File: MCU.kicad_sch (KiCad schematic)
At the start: 19 parts, among them IC3 MT2492, J1 FH34SRJ-8S-0.5SH_50_, U17 LD1117S33TR_SOT223

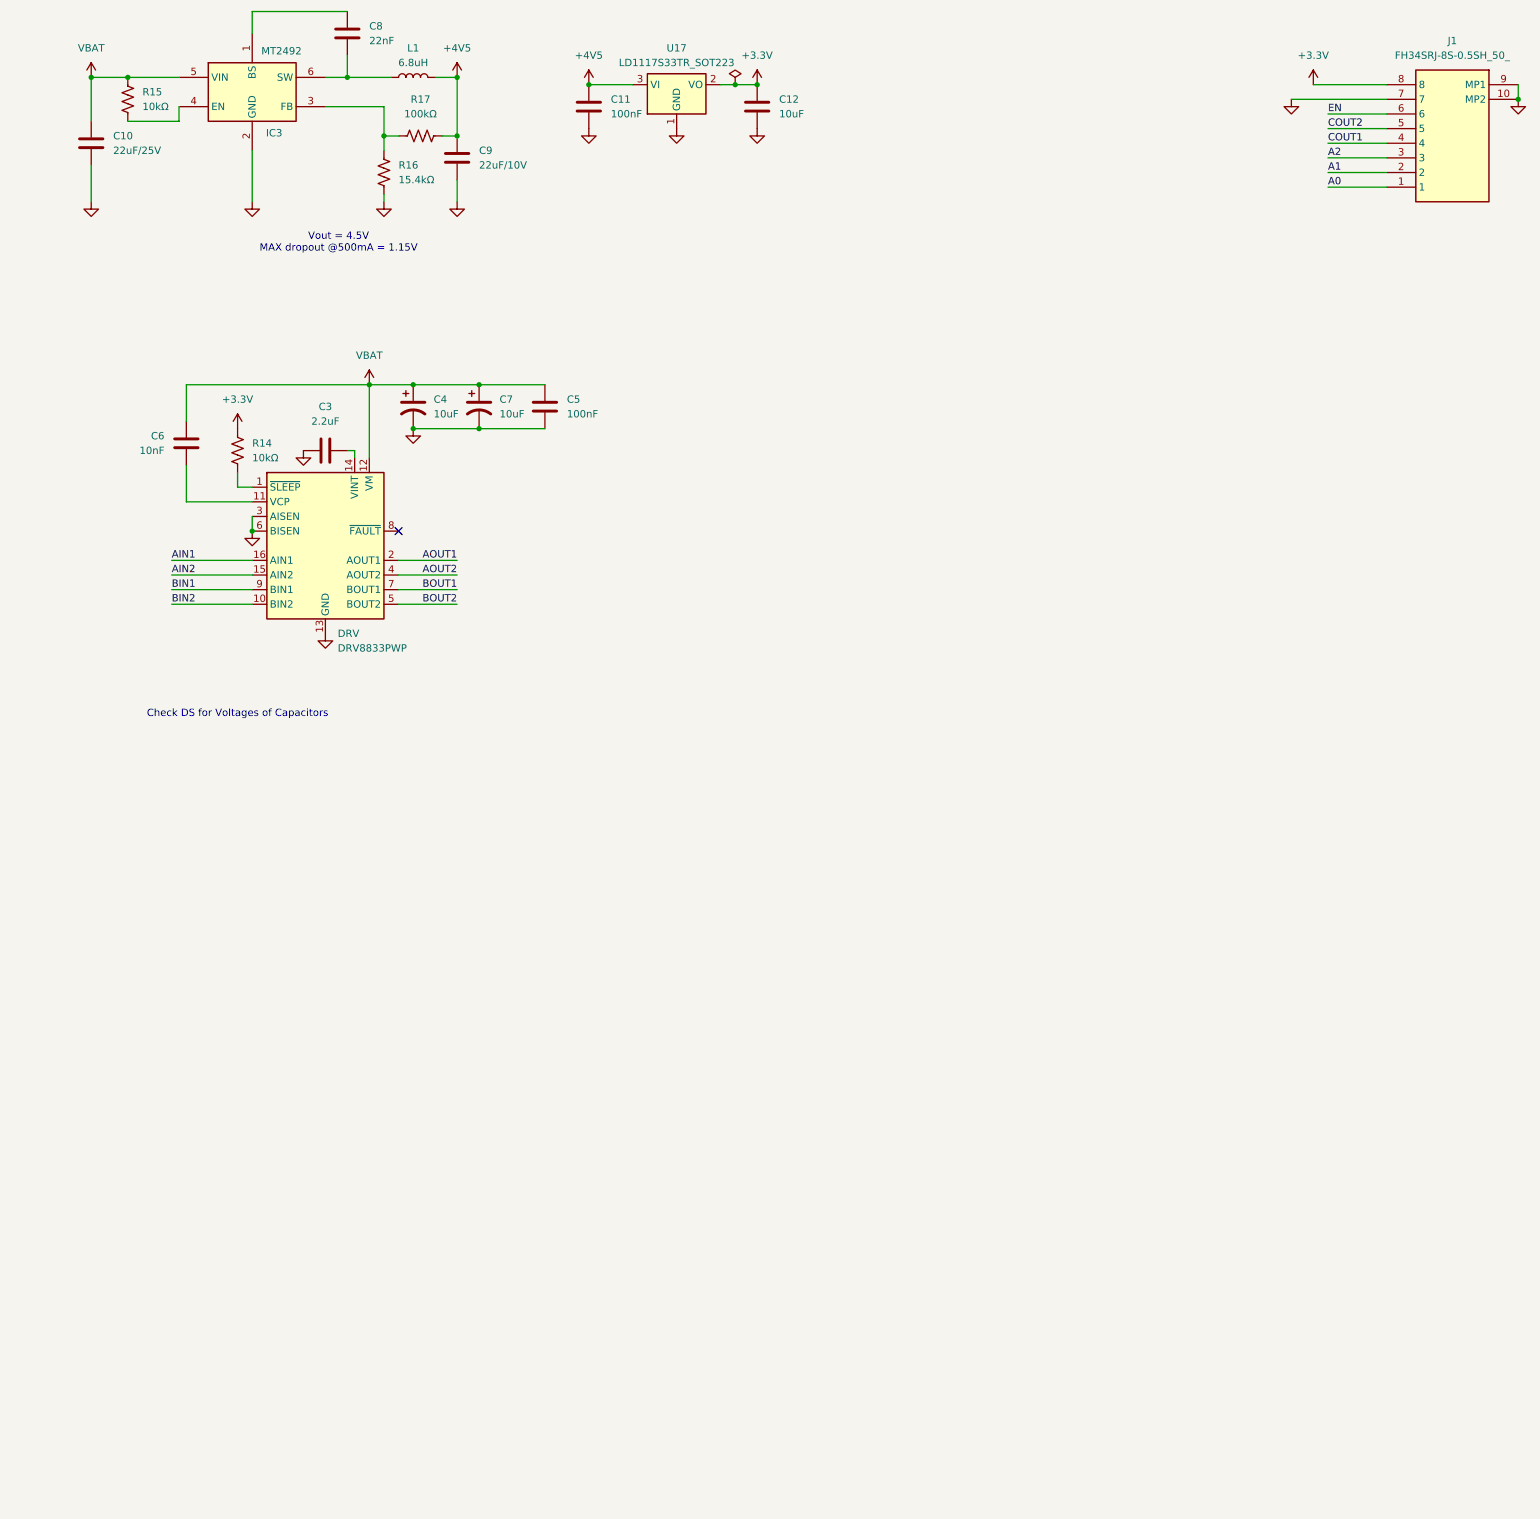
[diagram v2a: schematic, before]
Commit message: Changed motor driver from DRV8874 to a simpler, small-footprint DRV8837 using the IN1/IN2 interface.
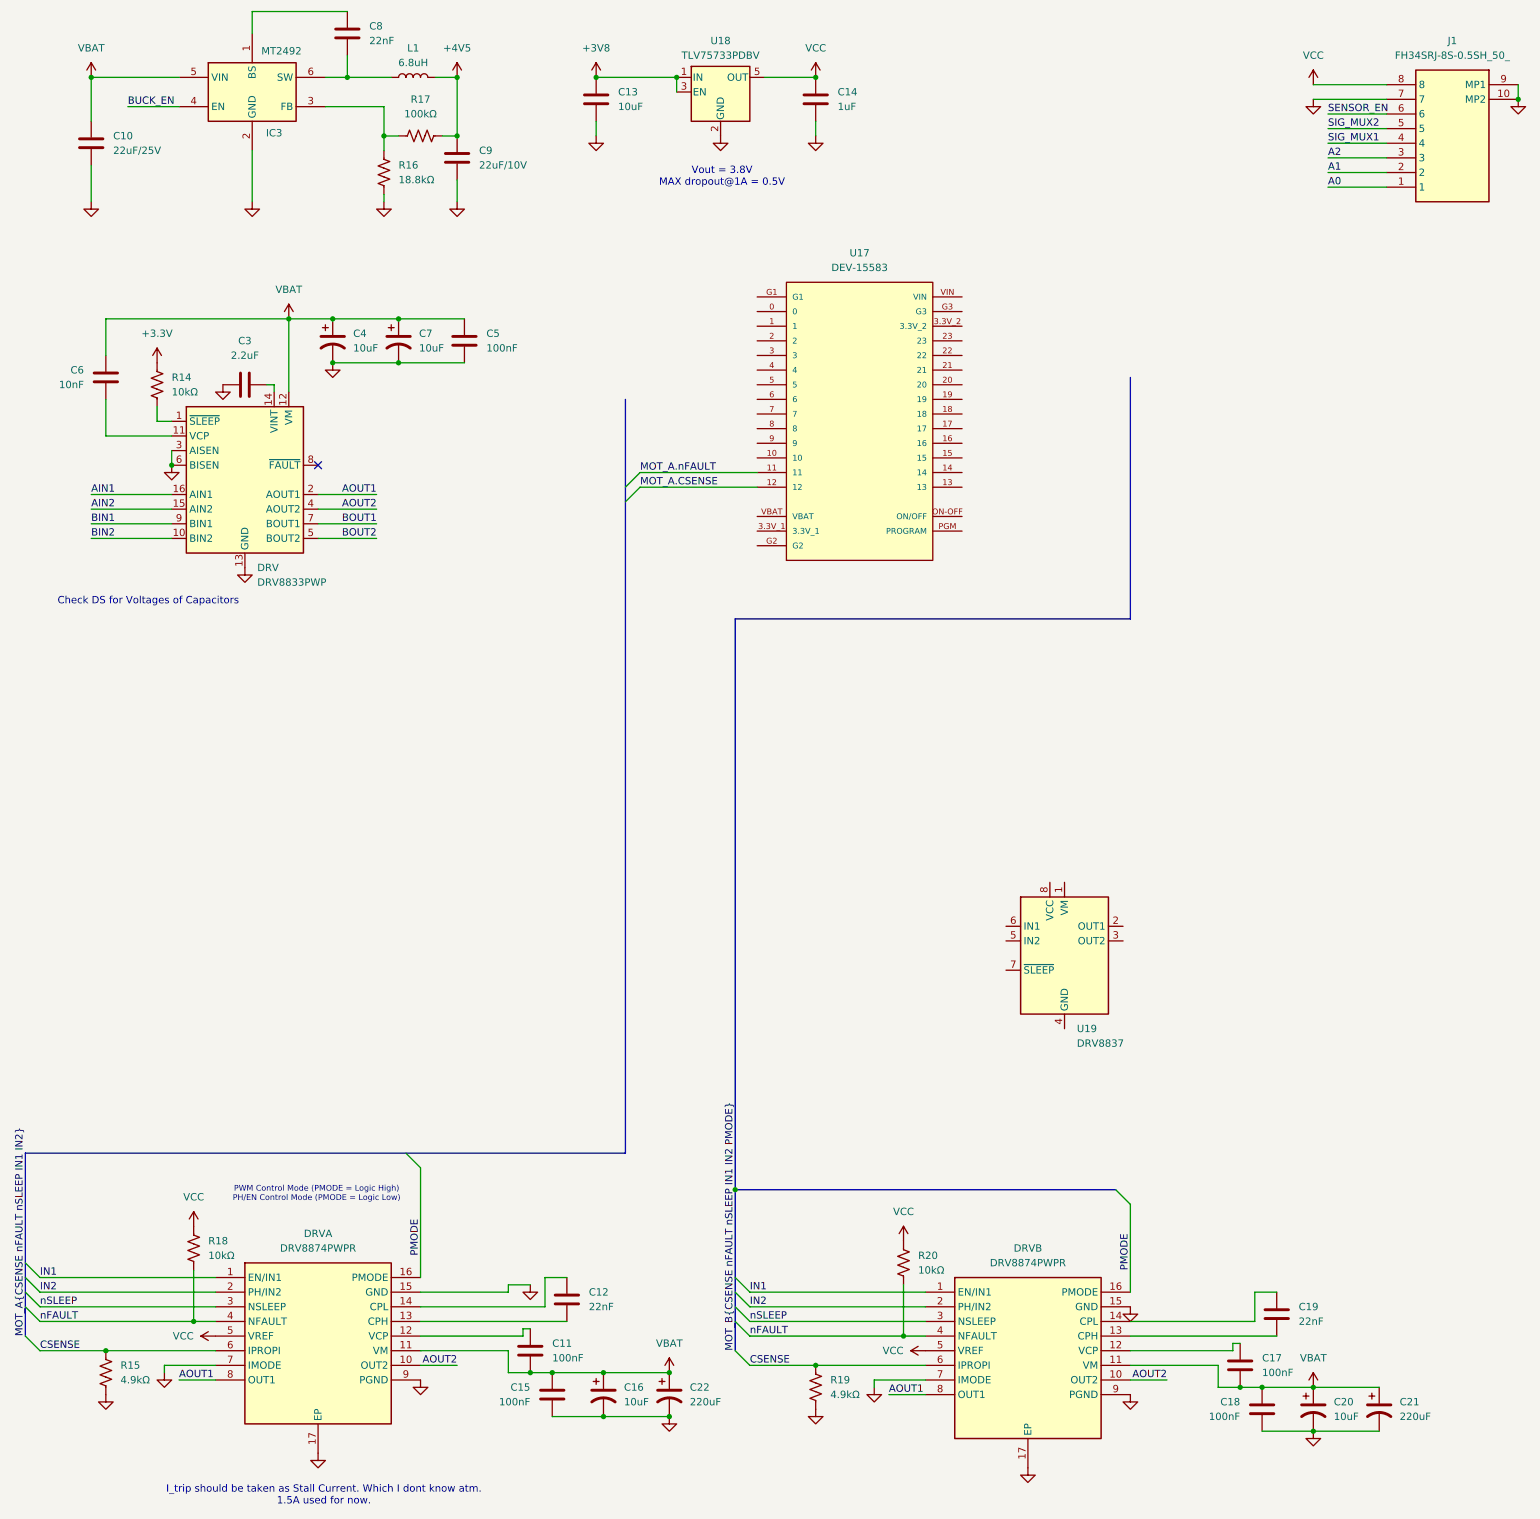
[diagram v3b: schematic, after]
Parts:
- removed U17: LD1117S33TR_SOT223, Package_TO_SOT_SMD:SOT-223-3_TabPin2, symbol Regulator_Linear:LD1117S33TR_SOT223
- added C13: 10uF, symbol Device:C
- added C14: 1uF, symbol Device:C
- added C15, C17, C18: 100nF, symbol Device:C
- added C16, C20: 10uF, symbol Device:C_Polarized_US
- added C19: 22nF, symbol Device:C
- added C21, C22: 220uF, symbol Device:C_Polarized_US
- added DRVA, DRVB: DRV8874PWPR, SAVITAR:SOP65P640X155-18N, symbol SAVITAR:DRV8874PWPR
- added R18, R20: 10kΩ, symbol Device:R_US
- added R19: 4.9kΩ, symbol Device:R_US
- added U17: DEV-15583, DEV-15583:MODULE_DEV-15583, symbol SAVITAR:DEV-15583
- added U18: TLV75733PDBV, Package_TO_SOT_SMD:SOT-23-5, symbol Regulator_Linear:TLV75733PDBV
- added U19: DRV8837, Package_SON:WSON-8-1EP_2x2mm_P0.5mm_EP0.9x1.6mm_ThermalVias, symbol Driver_Motor:DRV8837
- C12: value 10uF -> 22nF
- R15: value 10kΩ -> 4.9kΩ
- R16: value 15.4kΩ -> 18.8kΩ
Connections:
- net +3.3V: no longer C12.2, J1.8
- net +4V5: no longer C11.2
- net AOUT1: now also DRVA.8 (OUT1), DRVB.8 (OUT1)
- net AOUT2: now also DRVA.10 (OUT2), DRVB.10 (OUT2)
- net GND: now also R15.2, C13.1, C14.1, C15.1, C16.2, C18.1, C20.2, C21.2, C22.2, DRVA.15 (GND), DRVA.17 (EP), DRVA.7 (IMODE), DRVA.9 (PGND), DRVB.15 (GND), DRVB.17 (EP), DRVB.7 (IMODE), DRVB.9 (PGND), R19.2, U18.2 (GND); no longer C11.1, C12.1
- net VBAT: now also C11.1, C15.2, C16.1, C17.1, C18.2, C20.1, C21.1, C22.1, DRVA.11 (VM), DRVB.11 (VM); no longer R15.1
- net BUCK_EN: now reaches IC3.4 (EN)
- net BUCK_EN: no longer R15.2
- net COUT1 renamed SIG_MUX1
- net COUT2 renamed SIG_MUX2
- net EN renamed SENSOR_EN
- new net: C11.2, DRVA.12 (VCP)
- new net: C12.1, DRVA.13 (CPH)
- new net: C12.2, DRVA.14 (CPL)
- new net: C19.1, DRVB.13 (CPH)
- new net: C19.2, DRVB.14 (CPL)
- new net: C17.2, DRVB.12 (VCP)
- new net: U19.4 (GND), U19.9 (GND)
- new net +3V8: C13.2, U18.1 (IN), U18.3 (EN)
- new net CSENSE: DRVA.6 (IPROPI), DRVB.6 (IPROPI), R15.1, R19.1
- new net IN1: DRVA.1 (EN/IN1), DRVB.1 (EN/IN1)
- new net IN2: DRVA.2 (PH/IN2), DRVB.2 (PH/IN2)
- new net MOT_A.CSENSE: U17.12
- new net MOT_A.nFAULT: U17.11
- new net PMODE: DRVA.16 (PMODE), DRVB.16 (PMODE)
- new net VCC: C14.2, DRVA.5 (VREF), DRVB.5 (VREF), J1.8, R18.1, R20.1, U18.5 (OUT)
- new net nFAULT: DRVA.4 (NFAULT), DRVB.4 (NFAULT), R18.2, R20.2
- new net nSLEEP: DRVA.3 (NSLEEP), DRVB.3 (NSLEEP)
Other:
- note added: "I_trip should be taken as Stall Current. Which I dont know atm. 1.5A used for now."
- note added: "PWM Control Mode (PMODE = Logic High) PH/EN Control Mode (PMODE = Logic Low)"
- note added: "Vout = 3.8V MAX dropout@1A = 0.5V"
- note removed: "Vout = 4.5V MAX dropout @500mA = 1.15V"
- moved on the sheet: C3, C4, C5, C6, C7, DRV, R14

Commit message: Added ESP32-C3-MINI-1 circuit for the PD control over AP STA. Added comments and read sequence explanation. The schematic is finished, please add tag.
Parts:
- removed C16, C20, C4, C7: 10uF, symbol Device:C_Polarized_US
- removed C21, C22: 220uF, symbol Device:C_Polarized_US
- removed C3: 2.2uF, symbol Device:C
- removed C6: 10nF, symbol Device:C
- removed DRV: DRV8833PWP, Package_SO:HTSSOP-16-1EP_4.4x5mm_P0.65mm_EP3.4x5mm_Mask2.46x2.31mm_ThermalVias, symbol Driver_Motor:DRV8833PWP
- removed R14: 10kΩ, symbol Device:R_US
- removed U17: DEV-15583, DEV-15583:MODULE_DEV-15583, symbol SAVITAR:DEV-15583
- removed U19: DRV8837, Package_SON:WSON-8-1EP_2x2mm_P0.5mm_EP0.9x1.6mm_ThermalVias, symbol Driver_Motor:DRV8837
- added C11, C12: 100nF/50V, symbol Device:C
- added C13: 1uF/16V, symbol Device:C
- added C15: 22uF/25V, Capacitor_SMD:C_1206_3216Metric_Pad1.33x1.80mm_HandSolder, symbol Device:C
- added C18, C20, C21, C4, C7: 47uF, Capacitor_SMD:C_1206_3216Metric_Pad1.33x1.80mm_HandSolder, symbol Device:C
- added C22, C8: 47uF/25V, Capacitor_SMD:C_1206_3216Metric_Pad1.33x1.80mm_HandSolder, symbol Device:C
- added R10, R9: 470Ω, symbol Device:R_Small_US
- added R11, R3, R6, R8: 10kΩ, symbol Device:R_US
- added R12, R13: 0Ω, symbol Device:R_Small_US
- added R7: 10kΩ(1%), symbol Device:R_US
- added SWB1, SWEN1: TS-1088-AR02016, Button_Switch_SMD:SW_SPST_TS-1088-xR020, symbol Switch:SW_Push
- added TPA1, TPA2, TPB1, TPB2: TestPoint, TestPoint:TestPoint_THTPad_2.0x2.0mm_Drill1.0mm, symbol Connector:TestPoint
- added U1: TEENSY 4.0, SAVITAR:MODULE_DEV-15583, symbol SAVITAR:DEV-15583
- added U2: ESP32-C3-MINI-1-H4X, SAVITAR:ESP32C3MINI1H4X, symbol SAVITAR:ESP32-C3-MINI-1-H4X
- C1: renamed from C11; value 100nF -> 100nF/16V
- C10: renamed from C9; value 22uF/10V -> 22uF/16V
- C14: renamed from C17; value 100nF -> 100nF/16V
- C16: renamed from C18; value 100nF -> 100nF/50V
- C17: renamed from C19; value 22nF -> 22nF/50V
- C19: renamed from C13; value 10uF -> 10uF/25V
- C2: renamed from C15; value 100nF -> 100nF/50V
- C23: renamed from C14; value 1uF -> 2.2uF/25V
- C3: renamed from C12; value 22nF -> 22nF/50V
- C5: value 100nF -> 47uF; footprint (none) -> Capacitor_SMD:C_1206_3216Metric_Pad1.33x1.80mm_HandSolder
- IC1: renamed from IC3; footprint SOT95P280X145-6N -> SAVITAR:SOT95P280X145-6N
- J1: footprint FH34SRJ8S05SH50 -> SAVITAR:FH34SRJ8S05SH50
- R1: renamed from R15; value 4.9kΩ -> 2.7kΩ
- R4: renamed from R19; value 4.9kΩ -> 2.7kΩ
- RVD1: renamed from R16; value 18.8kΩ -> 18.7kΩ(1%)
- RVD2: renamed from R17; value 100kΩ -> 100kΩ(1%)
- renumbered C10 to C6, C8 to C9, DRVA to DRV1, DRVB to DRV2, R18 to R2, R20 to R5, U18 to U3
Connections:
- net +4V5 is gone; now on net +3V8: C10.1, L1.2, RVD2.2
- net BUCK_EN is gone; now on net VBAT: IC1.4 (EN)
- net +3V8: now also C12.2, U1.VIN
- net AOUT1: now also TPA1.1; no longer DRV2.8 (OUT1)
- net AOUT2: now also TPA2.1; no longer DRV2.10 (OUT2)
- net BOUT1: now also DRV2.8 (OUT1), TPB1.1
- net BOUT2: now also DRV2.10 (OUT2), TPB2.1
- net GND: now also C5.2, C11.1, C12.1, C13.1, C15.2, C18.2, C20.2, C21.2, C22.2, C4.2, C7.2, C8.2, SWB1.1, SWEN1.1, U1.G1, U1.G2, U1.G3, U2.1 (GND_1), U2.11 (GND_3), U2.14 (GND_4), U2.2 (GND_2), U2.36 (GND_5), U2.37 (GND_6), U2.38 (GND_7), U2.39 (GND_8), U2.40 (GND_9), U2.41 (GND_10), U2.42 (GND_11), U2.43 (GND_12), U2.44 (GND_13), U2.45 (GND_14), U2.46 (GND_15), U2.47 (GND_16), U2.48 (GND_17), U2.49 (GND_18), U2.50 (GND_19), U2.51 (GND_20), U2.52 (GND_21), U2.53 (GND_22), U2.54 (GND_23), U2.55 (GND_24), U2.56 (GND_25), U2.57 (GND_26), U2.58 (GND_27), U2.59 (GND_28), U2.60 (GND_29), U2.61 (GND_30); no longer C5.1
- net VBAT: now also C5.1, C18.1, C20.1, C21.1, C22.1, C4.1, C7.1, C8.1; no longer C5.2
- net VCC: now also C11.2, C15.1, R11.1, R3.1, R6.1, R7.1, R8.1, U2.3 (3V3)
- net A0 renamed SEN_A0
- net SEN_A0: now also U1.19
- net A1 renamed SEN_A1
- net SEN_A1: now also U1.18
- net A2 renamed SEN_A2
- net SEN_A2: now also U1.17
- net CSENSE renamed MOT_{A}.C_{SENSE}
- net MOT_{A}.C_{SENSE}: now also U1.23; no longer DRV2.6 (IPROPI), R4.1
- net IN1 renamed MOT_{A}.EN/IN1
- net MOT_{A}.EN/IN1: now also U1.2; no longer DRV2.1 (EN/IN1)
- net IN2 renamed MOT_{A}.PH/IN2
- net MOT_{A}.PH/IN2: now also U1.3; no longer DRV2.2 (PH/IN2)
- net PMODE renamed MOT_{A}.PMODE
- net MOT_{A}.PMODE: now also R3.2, U1.6; no longer DRV2.16 (PMODE)
- net SENSOR_EN renamed SEN_EN
- net SEN_EN: now also U1.12
- net SIG_MUX1 renamed SEN_MUX1
- net SEN_MUX1: now also U1.20
- net SIG_MUX2 renamed SEN_MUX2
- net SEN_MUX2: now also U1.21
- net nFAULT renamed MOT_{A}.~{FAULT}
- net MOT_{A}.~{FAULT}: now also U1.5; no longer DRV2.4 (NFAULT), R5.2
- net nSLEEP renamed MOT_{A}.~{SLEEP}
- net MOT_{A}.~{SLEEP}: now also U1.4; no longer DRV2.3 (NSLEEP)
- new net: R11.2, U2.22 (IO8)
- new net: R10.2, R13.1
- new net: R12.2, U2.30 (RXD0)
- new net: R13.2, U2.31 (TXD0)
- new net: R12.1, R9.2
- new net ESP_BOOT: R8.2, SWB1.2, U2.23 (IO9)
- new net ESP_EN: C13.2, R7.2, SWEN1.2, U2.8 (EN)
- new net MOT_{B}.C_{SENSE}: DRV2.6 (IPROPI), R4.1, U1.22
- new net MOT_{B}.EN/IN1: DRV2.1 (EN/IN1), U1.7
- new net MOT_{B}.PH/IN2: DRV2.2 (PH/IN2), U1.8
- new net MOT_{B}.PMODE: DRV2.16 (PMODE), R6.2, U1.11
- new net MOT_{B}.~{FAULT}: DRV2.4 (NFAULT), R5.2, U1.10
- new net MOT_{B}.~{SLEEP}: DRV2.3 (NSLEEP), U1.9
- new net TNS_RX1: R10.1, U1.0
- new net TNS_TX1: R9.1, U1.1
- no-connect marks 1 -> 34
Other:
- note added: "AP STA for PD Tuning"
- note added: "DC/DC BUCK"
- note added: "ESP32-C3-MINI-1"
- note added: "I_{trip} should be taken as Stall Current. Which I dont know atm. 2.5A used for now."
- note added: "LDO"
- note added: "MOTOR DRIVERS"
- note added: "POWER REGULATION"
- note added: "SENSOR ARRAY CONNECTOR"
- note added: "TEENSY 4"
- note added: "TODO: Cut between V_{USB} and V_{IN} Pad on the TEENSY 4 board."
- note added: "V_{FB} = 0.6V"
- note added: "V_{IN} = 3.6V .. 5.5V"
- note added: "V_{IPROPI}@2.5A Peak = 3.07V"
- note added: "V_{out} = 3.8V MAX dropout@1A = 0.5V"
- note added: "∆V_{OUT} = 4mV"
- note removed: "Check DS for Voltages of Capacitors"
- note removed: "I_trip should be taken as Stall Current. Which I dont know atm. 1.5A used for now."
- note removed: "Vout = 3.8V MAX dropout@1A = 0.5V"
- moved on the sheet: C1, C10, C14, C16, C17, C19, C2, C23, C3, C6, C9, DRV1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
